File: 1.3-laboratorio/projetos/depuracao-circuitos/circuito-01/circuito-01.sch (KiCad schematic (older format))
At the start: 17 parts, among them J1 Conn_01x07_Male, J2 Conn_01x07_Male, J3 Conn_01x07_Male, J4 Conn_01x07_Male, J5 Conn_01x07_Male, J6 Conn_01x07_Male, P1 CONN_01X02, SW1 SW_DIP_x04, U1 7400, U2 7400, U3 74LS386

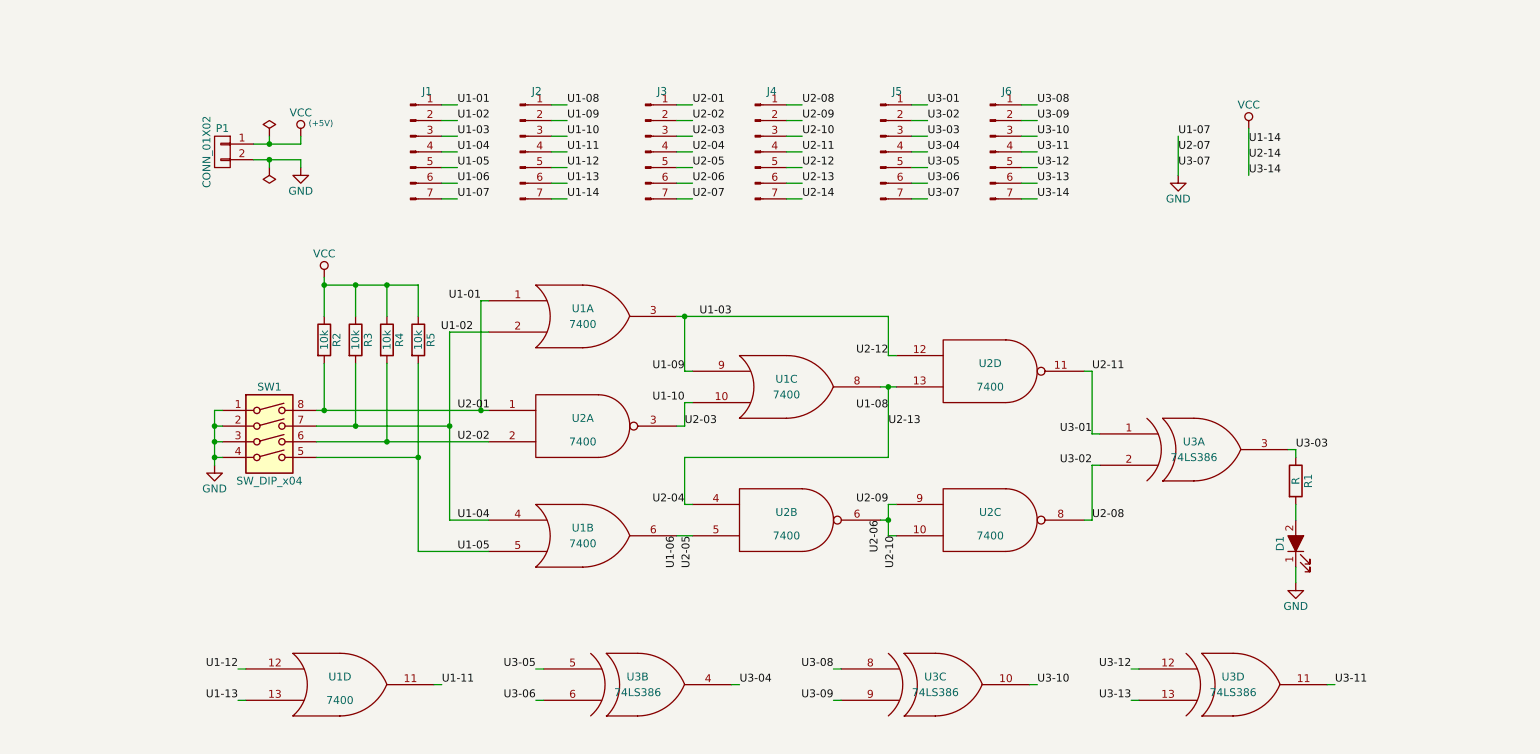
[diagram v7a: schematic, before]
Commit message: Posicionamento dos componentes na placa. Questão: diminuir a largura e aumentar o comprimento?
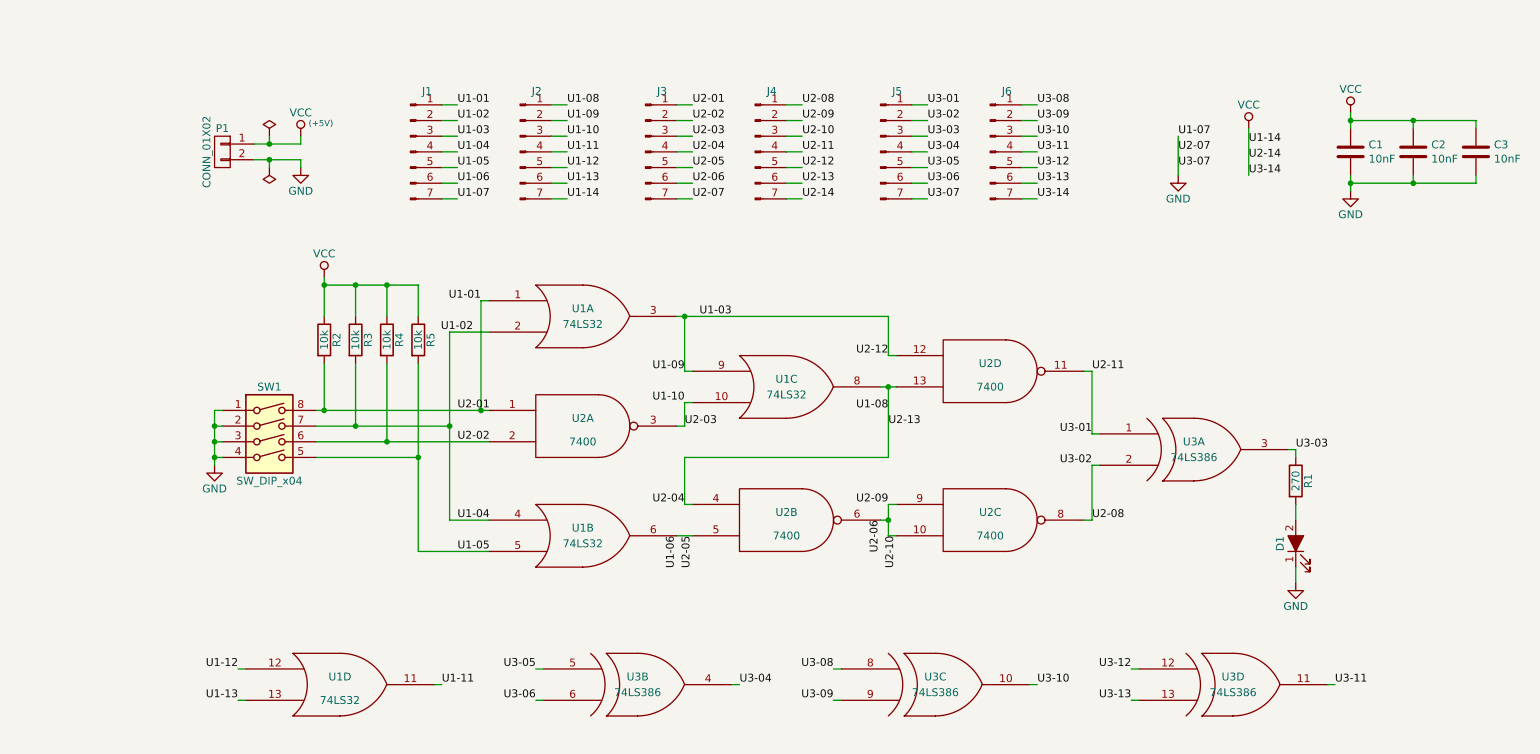
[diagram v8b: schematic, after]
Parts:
- added C1, C2, C3: 10nF, Capacitor_THT:C_Disc_D5.0mm_W2.5mm_P5.00mm, symbol Device:C
- D1: footprint (none) -> LED_THT:LED_D5.0mm
- J1, J2, J3, J4, J5, J6: footprint (none) -> Connector_PinHeader_2.54mm:PinHeader_1x07_P2.54mm_Vertical
- P1: footprint Terminal_Blocks:TerminalBlock_Altech_AK300-2_P5.00mm -> TerminalBlock_Altech:Altech_AK300_1x02_P5.00mm_45-Degree
- R1: value R -> 270; footprint Resistors_ThroughHole:R_Axial_DIN0207_L6.3mm_D2.5mm_P10.16mm_Horizontal -> Resistor_THT:R_Axial_DIN0207_L6.3mm_D2.5mm_P10.16mm_Horizontal
- R2, R3, R4, R5: footprint Resistors_ThroughHole:R_Axial_DIN0207_L6.3mm_D2.5mm_P10.16mm_Horizontal -> Resistor_THT:R_Axial_DIN0207_L6.3mm_D2.5mm_P10.16mm_Horizontal
- SW1: footprint Buttons_Switches_ThroughHole:SW_DIP_x4_W7.62mm_Slide -> Button_Switch_THT:SW_DIP_SPSTx04_Slide_9.78x12.34mm_W7.62mm_P2.54mm
- U1: value 7400 -> 74LS32; footprint Package_DIP:DIP-14_W7.62mm_LongPads -> Package_DIP:DIP-14_W7.62mm_Socket_LongPads
- U2, U3: footprint Package_DIP:DIP-14_W7.62mm_LongPads -> Package_DIP:DIP-14_W7.62mm_Socket_LongPads
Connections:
- net GND: now also C1.2, C2.2, C3.2
- net VCC: now also C1.1, C2.1, C3.1
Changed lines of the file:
@@
 F 0 "U2" H 4550 3750 50  0000 C CNN
 F 1 "7400" H 4550 3600 50  0000 C CNN
-F 2 "Package_DIP:DIP-14_W7.62mm_LongPads" H 4550 3700 50  0001 C CNN
+F 2 "Package_DIP:DIP-14_W7.62mm_Socket_LongPads" H 4550 3700 50  0001 C CNN
 F 3 "" H 4550 3700 50  0001 C CNN
 	1    4550 3700
@@
 F 0 "U2" H 7150 4350 50  0000 C CNN
 F 1 "7400" H 7150 4200 50  0000 C CNN
-F 2 "Package_DIP:DIP-14_W7.62mm_LongPads" H 7150 4300 50  0001 C CNN
+F 2 "Package_DIP:DIP-14_W7.62mm_Socket_LongPads" H 7150 4300 50  0001 C CNN
 F 3 "" H 7150 4300 50  0001 C CNN
 	3    7150 4300
@@
 F 0 "U2" H 7150 3400 50  0000 C CNN
 F 1 "7400" H 7150 3250 50  0000 C CNN
-F 2 "Package_DIP:DIP-14_W7.62mm_LongPads" H 7150 3350 50  0001 C CNN
+F 2 "Package_DIP:DIP-14_W7.62mm_Socket_LongPads" H 7150 3350 50  0001 C CNN
 F 3 "" H 7150 3350 50  0001 C CNN
 	4    7150 3350
@@
 P 4550 3000
 F 0 "U1" H 4550 3050 50  0000 C CNN
-F 1 "7400" H 4550 2950 50  0000 C CNN
-F 2 "Package_DIP:DIP-14_W7.62mm_LongPads" H 4550 3000 50  0001 C CNN
+F 1 "74LS32" H 4550 2950 50  0000 C CNN
+F 2 "Package_DIP:DIP-14_W7.62mm_Socket_LongPads" H 4550 3000 50  0001 C CNN
 F 3 "" H 4550 3000 50  0001 C CNN
 	1    4550 3000
@@
 P 4550 4400
 F 0 "U1" H 4550 4450 50  0000 C CNN
-F 1 "7400" H 4550 4350 50  0000 C CNN
-F 2 "Package_DIP:DIP-14_W7.62mm_LongPads" H 4550 4400 50  0001 C CNN
+F 1 "74LS32" H 4550 4350 50  0000 C CNN
+F 2 "Package_DIP:DIP-14_W7.62mm_Socket_LongPads" H 4550 4400 50  0001 C CNN
 F 3 "" H 4550 4400 50  0001 C CNN
 	2    4550 4400
@@
 P 5850 3450
 F 0 "U1" H 5850 3500 50  0000 C CNN
-F 1 "7400" H 5850 3400 50  0000 C CNN
-F 2 "Package_DIP:DIP-14_W7.62mm_LongPads" H 5850 3450 50  0001 C CNN
+F 1 "74LS32" H 5850 3400 50  0000 C CNN
+F 2 "Package_DIP:DIP-14_W7.62mm_Socket_LongPads" H 5850 3450 50  0001 C CNN
 F 3 "" H 5850 3450 50  0001 C CNN
 	3    5850 3450
@@
 F 0 "U3" H 8450 3900 50  0000 C CNN
 F 1 "74LS386" H 8450 3800 50  0000 C CNN
-F 2 "Package_DIP:DIP-14_W7.62mm_LongPads" H 8450 3850 50  0001 C CNN
+F 2 "Package_DIP:DIP-14_W7.62mm_Socket_LongPads" H 8450 3850 50  0001 C CNN
 F 3 "" H 8450 3850 50  0001 C CNN
 	1    8450 3850
@@
 P 9100 4050
 F 0 "R1" V 9180 4050 50  0000 C CNN
-F 1 "R" V 9100 4050 50  0000 C CNN
-F 2 "Resistors_ThroughHole:R_Axial_DIN0207_L6.3mm_D2.5mm_P10.16mm_Horizontal" V 9030 4050 50  0001 C CNN
+F 1 "270" V 9100 4050 50  0000 C CNN
+F 2 "Resistor_THT:R_Axial_DIN0207_L6.3mm_D2.5mm_P10.16mm_Horizontal" V 9030 4050 50  0001 C CNN
 F 3 "" H 9100 4050 50  0001 C CNN
 	1    9100 4050
@@
 F 0 "R2" V 2980 3150 50  0000 C CNN
 F 1 "10k" V 2900 3150 50  0000 C CNN
-F 2 "Resistors_ThroughHole:R_Axial_DIN0207_L6.3mm_D2.5mm_P10.16mm_Horizontal" V 2830 3150 50  0001 C CNN
+F 2 "Resistor_THT:R_Axial_DIN0207_L6.3mm_D2.5mm_P10.16mm_Horizontal" V 2830 3150 50  0001 C CNN
 F 3 "" H 2900 3150 50  0001 C CNN
 	1    2900 3150
@@
 F 0 "R3" V 3180 3150 50  0000 C CNN
 F 1 "10k" V 3100 3150 50  0000 C CNN
-F 2 "Resistors_ThroughHole:R_Axial_DIN0207_L6.3mm_D2.5mm_P10.16mm_Horizontal" V 3030 3150 50  0001 C CNN
+F 2 "Resistor_THT:R_Axial_DIN0207_L6.3mm_D2.5mm_P10.16mm_Horizontal" V 3030 3150 50  0001 C CNN
 F 3 "" H 3100 3150 50  0001 C CNN
 	1    3100 3150
@@
 F 0 "R4" V 3380 3150 50  0000 C CNN
 F 1 "10k" V 3300 3150 50  0000 C CNN
-F 2 "Resistors_ThroughHole:R_Axial_DIN0207_L6.3mm_D2.5mm_P10.16mm_Horizontal" V 3230 3150 50  0001 C CNN
+F 2 "Resistor_THT:R_Axial_DIN0207_L6.3mm_D2.5mm_P10.16mm_Horizontal" V 3230 3150 50  0001 C CNN
 F 3 "" H 3300 3150 50  0001 C CNN
 	1    3300 3150
@@
 F 0 "R5" V 3580 3150 50  0000 C CNN
 F 1 "10k" V 3500 3150 50  0000 C CNN
-F 2 "Resistors_ThroughHole:R_Axial_DIN0207_L6.3mm_D2.5mm_P10.16mm_Horizontal" V 3430 3150 50  0001 C CNN
+F 2 "Resistor_THT:R_Axial_DIN0207_L6.3mm_D2.5mm_P10.16mm_Horizontal" V 3430 3150 50  0001 C CNN
 F 3 "" H 3500 3150 50  0001 C CNN
 	1    3500 3150
@@
 F 0 "SW1" H 2550 4150 50  0000 C CNN
 F 1 "SW_DIP_x04" H 2550 3550 50  0000 C CNN
-F 2 "Buttons_Switches_ThroughHole:SW_DIP_x4_W7.62mm_Slide" H 2550 3800 50  0001 C CNN
+F 2 "Button_Switch_THT:SW_DIP_SPSTx04_Slide_9.78x12.34mm_W7.62mm_P2.54mm" H 2550 3800 50  0001 C CNN
 F 3 "" H 2550 3800 50  0001 C CNN
 	1    2550 3800
@@
 F 0 "P1" H 2250 2100 50  0000 C CNN
 F 1 "CONN_01X02" V 2350 1950 50  0000 C CNN
-F 2 "Terminal_Blocks:TerminalBlock_Altech_AK300-2_P5.00mm" H 2250 1950 50  0001 C CNN
+F 2 "TerminalBlock_Altech:Altech_AK300_1x02_P5.00mm_45-Degree" H 2250 1950 50  0001 C CNN
 F 3 "" H 2250 1950 50  0000 C CNN
 	1    2250 1950
@@
 F 0 "D1" H 9100 4550 50  0000 C CNN
 F 1 "LED_ALT" H 9100 4350 50  0001 C CNN
-F 2 "" H 9100 4450 50  0001 C CNN
+F 2 "LED_THT:LED_D5.0mm" H 9100 4450 50  0001 C CNN
 F 3 "" H 9100 4450 50  0001 C CNN
 	1    9100 4450
@@
 F 0 "J1" H 3556 2337 50  0000 C CNN
 F 1 "Conn_01x07_Male" H 3556 2337 50  0001 C CNN
-F 2 "" H 3450 1950 50  0001 C CNN
+F 2 "Connector_PinHeader_2.54mm:PinHeader_1x07_P2.54mm_Vertical" H 3450 1950 50  0001 C CNN
 F 3 "~" H 3450 1950 50  0001 C CNN
 	1    3450 1950
@@
 F 0 "J2" H 4256 2337 50  0000 C CNN
 F 1 "Conn_01x07_Male" H 4256 2337 50  0001 C CNN
-F 2 "" H 4150 1950 50  0001 C CNN
+F 2 "Connector_PinHeader_2.54mm:PinHeader_1x07_P2.54mm_Vertical" H 4150 1950 50  0001 C CNN
 F 3 "~" H 4150 1950 50  0001 C CNN
 	1    4150 1950
@@
 F 0 "J3" H 5056 2337 50  0000 C CNN
 F 1 "Conn_01x07_Male" H 5056 2337 50  0001 C CNN
-F 2 "" H 4950 1950 50  0001 C CNN
+F 2 "Connector_PinHeader_2.54mm:PinHeader_1x07_P2.54mm_Vertical" H 4950 1950 50  0001 C CNN
 F 3 "~" H 4950 1950 50  0001 C CNN
 	1    4950 1950
@@
 F 0 "J4" H 5756 2337 50  0000 C CNN
 F 1 "Conn_01x07_Male" H 5756 2337 50  0001 C CNN
-F 2 "" H 5650 1950 50  0001 C CNN
+F 2 "Connector_PinHeader_2.54mm:PinHeader_1x07_P2.54mm_Vertical" H 5650 1950 50  0001 C CNN
 F 3 "~" H 5650 1950 50  0001 C CNN
 	1    5650 1950
@@
 F 0 "J5" H 6556 2337 50  0000 C CNN
 F 1 "Conn_01x07_Male" H 6556 2337 50  0001 C CNN
-F 2 "" H 6450 1950 50  0001 C CNN
+F 2 "Connector_PinHeader_2.54mm:PinHeader_1x07_P2.54mm_Vertical" H 6450 1950 50  0001 C CNN
 F 3 "~" H 6450 1950 50  0001 C CNN
 	1    6450 1950
@@
 F 0 "J6" H 7256 2337 50  0000 C CNN
 F 1 "Conn_01x07_Male" H 7256 2337 50  0001 C CNN
-F 2 "" H 7150 1950 50  0001 C CNN
+F 2 "Connector_PinHeader_2.54mm:PinHeader_1x07_P2.54mm_Vertical" H 7150 1950 50  0001 C CNN
 F 3 "~" H 7150 1950 50  0001 C CNN
 	1    7150 1950
@@
 F 0 "U2" H 5850 4350 50  0000 C CNN
 F 1 "7400" H 5850 4200 50  0000 C CNN
-F 2 "Package_DIP:DIP-14_W7.62mm_LongPads" H 5850 4300 50  0001 C CNN
+F 2 "Package_DIP:DIP-14_W7.62mm_Socket_LongPads" H 5850 4300 50  0001 C CNN
 F 3 "" H 5850 4300 50  0001 C CNN
 	2    5850 4300
@@
 P 3000 5350
 F 0 "U1" H 3000 5400 50  0000 C CNN
-F 1 "7400" H 3000 5250 50  0000 C CNN
-F 2 "Package_DIP:DIP-14_W7.62mm_LongPads" H 3000 5350 50  0001 C CNN
+F 1 "74LS32" H 3000 5250 50  0000 C CNN
+F 2 "Package_DIP:DIP-14_W7.62mm_Socket_LongPads" H 3000 5350 50  0001 C CNN
 F 3 "" H 3000 5350 50  0001 C CNN
 	4    3000 5350
@@
 F 0 "U3" H 4900 5400 50  0000 C CNN
 F 1 "74LS386" H 4900 5300 50  0000 C CNN
-F 2 "Package_DIP:DIP-14_W7.62mm_LongPads" H 4900 5350 50  0001 C CNN
+F 2 "Package_DIP:DIP-14_W7.62mm_Socket_LongPads" H 4900 5350 50  0001 C CNN
 F 3 "" H 4900 5350 50  0001 C CNN
 	2    4900 5350
@@
 F 0 "U3" H 6800 5400 50  0000 C CNN
 F 1 "74LS386" H 6800 5300 50  0000 C CNN
-F 2 "Package_DIP:DIP-14_W7.62mm_LongPads" H 6800 5350 50  0001 C CNN
+F 2 "Package_DIP:DIP-14_W7.62mm_Socket_LongPads" H 6800 5350 50  0001 C CNN
 F 3 "" H 6800 5350 50  0001 C CNN
 	3    6800 5350
@@
 F 0 "U3" H 8700 5400 50  0000 C CNN
 F 1 "74LS386" H 8700 5300 50  0000 C CNN
-F 2 "Package_DIP:DIP-14_W7.62mm_LongPads" H 8700 5350 50  0001 C CNN
+F 2 "Package_DIP:DIP-14_W7.62mm_Socket_LongPads" H 8700 5350 50  0001 C CNN
 F 3 "" H 8700 5350 50  0001 C CNN
 	4    8700 5350
@@
 Text Label 5550 5350 0    50   ~ 0
 U3-04
+$Comp
+L circuito-01-rescue:VCC #PWR0103
+U 1 1 5CBEF2FF
+P 9450 1700
+F 0 "#PWR0103" H 9450 1550 50  0001 C CNN
+F 1 "VCC" H 9450 1850 50  0000 C CNN
+F 2 "" H 9450 1700 50  0000 C CNN
+F 3 "" H 9450 1700 50  0000 C CNN
+	1    9450 1700
+	1    0    0    -1
+$EndComp
+$Comp
+L circuito-01-rescue:GND #PWR0104
+U 1 1 5CBEF33E
+P 9450 2200
+F 0 "#PWR0104" H 9450 1950 50  0001 C CNN
+F 1 "GND" H 9450 2050 50  0000 C CNN
+F 2 "" H 9450 2200 50  0000 C CNN
+F 3 "" H 9450 2200 50  0000 C CNN
+	1    9450 2200
+	1    0    0    -1
+$EndComp
+$Comp
+L Device:C C1
+U 1 1 5CBEF386
+P 9450 1950
+F 0 "C1" H 9565 1996 50  0000 L CNN
+F 1 "10nF" H 9565 1905 50  0000 L CNN
+F 2 "Capacitor_THT:C_Disc_D5.0mm_W2.5mm_P5.00mm" H 9488 1800 50  0001 C CNN
+F 3 "~" H 9450 1950 50  0001 C CNN
+F 4 "Para U1." H 9450 1950 50  0001 C CNN "Observacao"
+	1    9450 1950
+	1    0    0    -1
+$EndComp
+Wire Wire Line
+	9450 1700 9450 1750
+Wire Wire Line
+	9450 2100 9450 2150
+Connection ~ 9450 1750
+Wire Wire Line
+	9450 1750 9450 1800
+Connection ~ 9450 2150
+Wire Wire Line
+	9450 2150 9450 2200
+$Comp
+L Device:C C2
+U 1 1 5CC2315F
+P 9850 1950
+F 0 "C2" H 9965 1996 50  0000 L CNN
+F 1 "10nF" H 9965 1905 50  0000 L CNN
+F 2 "Capacitor_THT:C_Disc_D5.0mm_W2.5mm_P5.00mm" H 9888 1800 50  0001 C CNN
+F 3 "~" H 9850 1950 50  0001 C CNN
+F 4 "Para U2." H 9850 1950 50  0001 C CNN "Observacao"
+	1    9850 1950
+	1    0    0    -1
+$EndComp
+$Comp
+L Device:C C3
+U 1 1 5CC231B3
+P 10250 1950
+F 0 "C3" H 10365 1996 50  0000 L CNN
+F 1 "10nF" H 10365 1905 50  0000 L CNN
+F 2 "Capacitor_THT:C_Disc_D5.0mm_W2.5mm_P5.00mm" H 10288 1800 50  0001 C CNN
+F 3 "~" H 10250 1950 50  0001 C CNN
+F 4 "Para U3." H 10250 1950 50  0001 C CNN "Observacao"
+	1    10250 1950
+	1    0    0    -1
+$EndComp
+Wire Wire Line
+	10250 1750 10250 1800
+Wire Wire Line
+	9450 1750 9850 1750
+Wire Wire Line
+	10250 2150 10250 2100
+Wire Wire Line
+	9450 2150 9850 2150
+Wire Wire Line
+	9850 2100 9850 2150
+Connection ~ 9850 2150
+Wire Wire Line
+	9850 2150 10250 2150
+Wire Wire Line
+	9850 1800 9850 1750
+Connection ~ 9850 1750
+Wire Wire Line
+	9850 1750 10250 1750
 $EndSCHEMATC
